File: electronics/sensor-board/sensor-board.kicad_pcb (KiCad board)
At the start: 2 copper layers, 270 x 30 mm, 0 parts

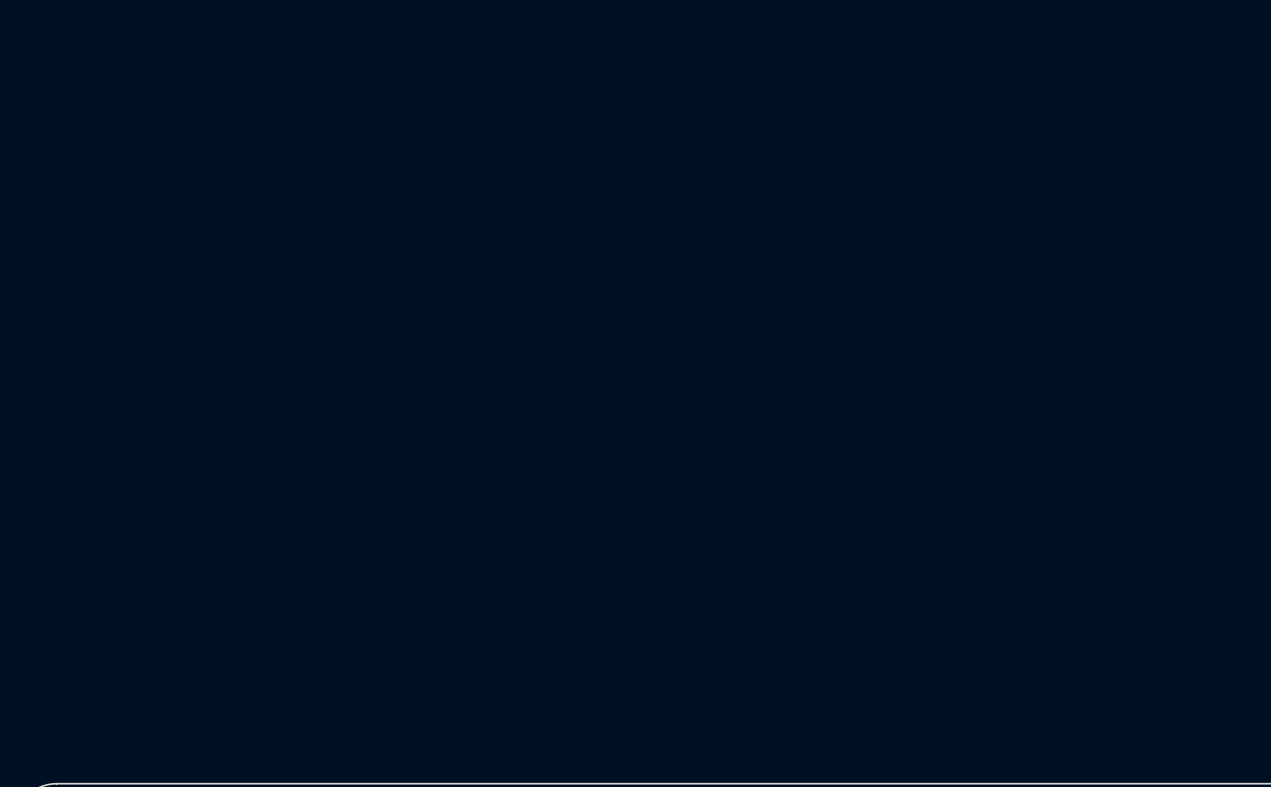
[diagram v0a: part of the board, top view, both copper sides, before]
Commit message: Minor tweaks, footprints added
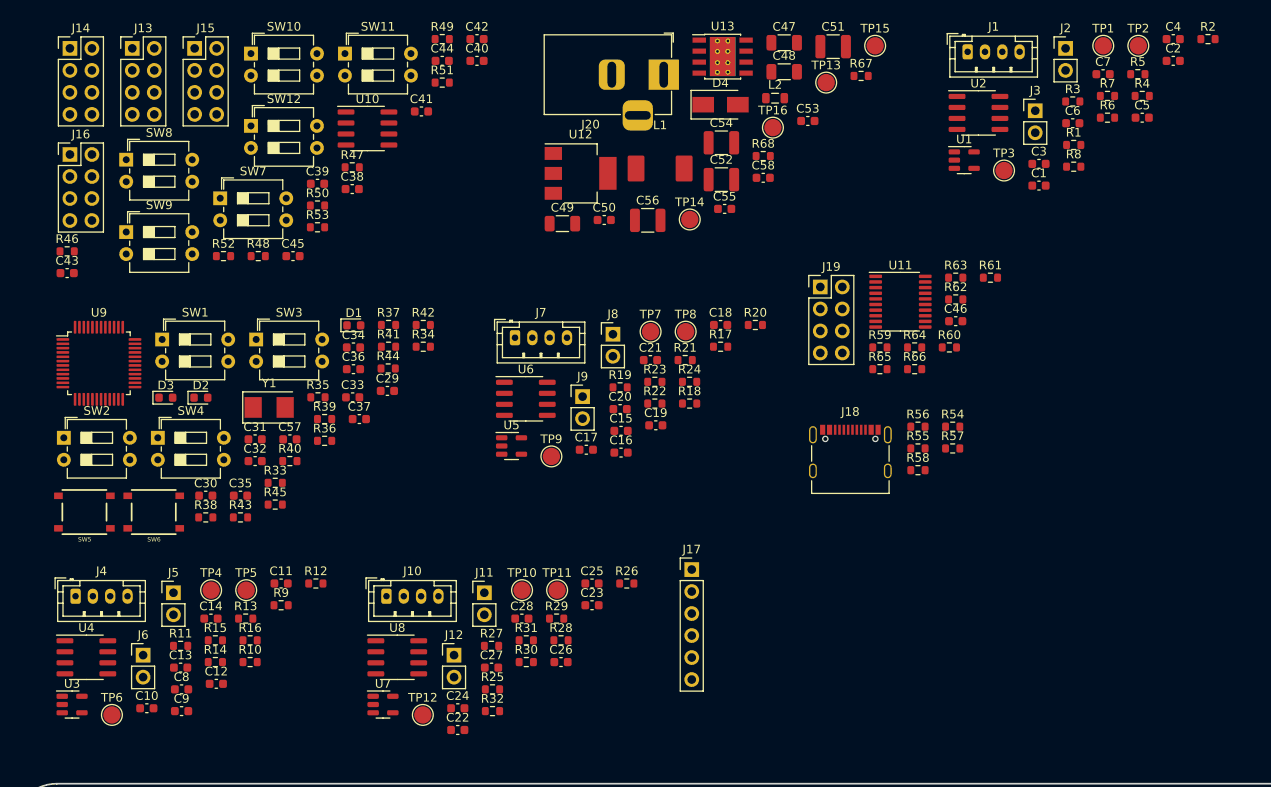
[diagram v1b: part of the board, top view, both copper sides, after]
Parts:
- added C1: 100n, Capacitor_SMD:C_0603_1608Metric, F.Cu at (196.0, 54.4)
- added C10: 4.7n, Capacitor_SMD:C_0603_1608Metric, F.Cu at (93.0, 114.7)
- added C11: 470n, Capacitor_SMD:C_0603_1608Metric, F.Cu at (108.5, 100.3)
- added C12: 4.7n, Capacitor_SMD:C_0603_1608Metric, F.Cu at (101.0, 111.9)
- added C13: 100n, Capacitor_SMD:C_0603_1608Metric, F.Cu at (96.9, 110.0)
- added C14: 10u, Capacitor_SMD:C_0603_1608Metric, F.Cu at (100.4, 104.3)
- added C15: 100n, Capacitor_SMD:C_0603_1608Metric, F.Cu at (147.7, 82.7)
- added C16: 100n, Capacitor_SMD:C_0603_1608Metric, F.Cu at (147.7, 85.2)
- added C17: 4.7n, Capacitor_SMD:C_0603_1608Metric, F.Cu at (143.7, 84.8)
- added C18: 470n, Capacitor_SMD:C_0603_1608Metric, F.Cu at (159.2, 70.5)
- added C19: 4.7n, Capacitor_SMD:C_0603_1608Metric, F.Cu at (151.7, 82.0)
- added C2: 100n, Capacitor_SMD:C_0603_1608Metric, F.Cu at (211.5, 40.0)
- added C20: 100n, Capacitor_SMD:C_0603_1608Metric, F.Cu at (147.6, 80.2)
- added C21: 10u, Capacitor_SMD:C_0603_1608Metric, F.Cu at (151.1, 74.5)
- added C22: 100n, Capacitor_SMD:C_0603_1608Metric, F.Cu at (128.9, 117.2)
- added C23: 100n, Capacitor_SMD:C_0603_1608Metric, F.Cu at (144.4, 102.8)
- added C24: 4.7n, Capacitor_SMD:C_0603_1608Metric, F.Cu at (128.9, 114.7)
- added C25: 470n, Capacitor_SMD:C_0603_1608Metric, F.Cu at (144.4, 100.3)
- added C26: 4.7n, Capacitor_SMD:C_0603_1608Metric, F.Cu at (140.8, 109.4)
- added C27: 100n, Capacitor_SMD:C_0603_1608Metric, F.Cu at (132.8, 110.0)
- added C28: 10u, Capacitor_SMD:C_0603_1608Metric, F.Cu at (136.3, 104.3)
- added C29: 22p, Capacitor_SMD:C_0603_1608Metric, F.Cu at (120.8, 78.1)
- added C3: 4.7n, Capacitor_SMD:C_0603_1608Metric, F.Cu at (196.0, 51.9)
- added C30: 22p, Capacitor_SMD:C_0603_1608Metric, F.Cu at (99.8, 90.2)
- added C31: 100n, Capacitor_SMD:C_0603_1608Metric, F.Cu at (105.5, 83.7)
- added C32: 100n, Capacitor_SMD:C_0603_1608Metric, F.Cu at (105.5, 86.2)
- added C33: 100n, Capacitor_SMD:C_0603_1608Metric, F.Cu at (116.7, 78.8)
- added C34: 470n, Capacitor_SMD:C_0603_1608Metric, F.Cu at (116.8, 73.0)
- added C35: 100n, Capacitor_SMD:C_0603_1608Metric, F.Cu at (103.8, 90.2)
- added C36: 100n, Capacitor_SMD:C_0603_1608Metric, F.Cu at (116.8, 75.5)
- added C37: 4.7u, Capacitor_SMD:C_0603_1608Metric, F.Cu at (117.5, 81.3)
- added C38: 100n, Capacitor_SMD:C_0603_1608Metric, F.Cu at (116.7, 54.8)
- added C39: 100n, Capacitor_SMD:C_0603_1608Metric, F.Cu at (112.7, 54.1)
- added C4: 470n, Capacitor_SMD:C_0603_1608Metric, F.Cu at (211.5, 37.5)
- added C40: 100p, Capacitor_SMD:C_0603_1608Metric, F.Cu at (131.1, 40.0)
- added C41: 4.7n, Capacitor_SMD:C_0603_1608Metric, F.Cu at (124.7, 45.8)
- added C42: 100p, Capacitor_SMD:C_0603_1608Metric, F.Cu at (131.1, 37.5)
- added C43: 100p, Capacitor_SMD:C_0603_1608Metric, F.Cu at (83.8, 64.5)
- added C44: 4.7n, Capacitor_SMD:C_0603_1608Metric, F.Cu at (127.1, 40.0)
- added C45: 100p, Capacitor_SMD:C_0603_1608Metric, F.Cu at (109.9, 62.5)
- added C46: 100n, Capacitor_SMD:C_0603_1608Metric, F.Cu at (186.4, 70.0)
- added C47: 10u, Capacitor_SMD:C_1206_3216Metric, F.Cu at (166.6, 37.9)
- added C48: 10u, Capacitor_SMD:C_1206_3216Metric, F.Cu at (166.6, 41.2)
- added C49: 22u, Capacitor_SMD:C_1206_3216Metric, F.Cu at (141.0, 58.8)
- added C5: 4.7n, Capacitor_SMD:C_0603_1608Metric, F.Cu at (207.9, 46.5)
- added C50: 100n, Capacitor_SMD:C_0603_1608Metric, F.Cu at (145.8, 58.3)
- added C51: 100u, Capacitor_SMD:C_1210_3225Metric, F.Cu at (172.2, 38.3)
- added C52: 100u, Capacitor_SMD:C_1210_3225Metric, F.Cu at (159.3, 53.7)
- added C53: 470n, Capacitor_SMD:C_0603_1608Metric, F.Cu at (169.3, 46.9)
- added C54: 100u, Capacitor_SMD:C_1210_3225Metric, F.Cu at (159.3, 49.4)
- added C55: 100n, Capacitor_SMD:C_0603_1608Metric, F.Cu at (159.7, 57.0)
- added C56: 100u, Capacitor_SMD:C_1210_3225Metric, F.Cu at (150.8, 58.4)
- added C57: 470n, Capacitor_SMD:C_0603_1608Metric, F.Cu at (109.5, 83.7)
- added C58: 470n, Capacitor_SMD:C_0603_1608Metric, F.Cu at (164.1, 53.5)
- added C6: 100n, Capacitor_SMD:C_0603_1608Metric, F.Cu at (199.9, 47.2)
- added C7: 10u, Capacitor_SMD:C_0603_1608Metric, F.Cu at (203.4, 41.5)
- added C8: 100n, Capacitor_SMD:C_0603_1608Metric, F.Cu at (97.0, 112.5)
- added C9: 100n, Capacitor_SMD:C_0603_1608Metric, F.Cu at (97.0, 115.0)
- added D1: Blue, LED_SMD:LED_0603_1608Metric, F.Cu at (116.9, 70.5)
- added D2: Green, LED_SMD:LED_0603_1608Metric, F.Cu at (99.2, 78.8)
- added D3: Yellow, LED_SMD:LED_0603_1608Metric, F.Cu at (95.2, 78.8)
- added D4: D_Schottky_Small, Diode_SMD:D_SMA, F.Cu at (159.2, 45.0)
- added J1: Load Cell Input, Connector_JST:JST_PH_B4B-PH-K_1x04_P2.00mm_Vertical, F.Cu at (187.7, 38.9)
- added J10: Load Cell Input, Connector_JST:JST_PH_B4B-PH-K_1x04_P2.00mm_Vertical, F.Cu at (120.6, 101.8)
- added J11: FSR Input, Connector_PinHeader_2.54mm:PinHeader_1x02_P2.54mm_Vertical, F.Cu at (131.9, 101.4)
- added J12: Digital Input, Connector_PinHeader_2.54mm:PinHeader_1x02_P2.54mm_Vertical, F.Cu at (128.4, 108.6)
- added J13: Conn_02x04_Counter_Clockwise, Connector_PinHeader_2.54mm:PinHeader_2x04_P2.54mm_Vertical, F.Cu at (91.3, 38.5)
- added J14: Conn_02x04_Counter_Clockwise, Connector_PinHeader_2.54mm:PinHeader_2x04_P2.54mm_Vertical, F.Cu at (84.1, 38.5)
- added J15: Conn_02x04_Counter_Clockwise, Connector_PinHeader_2.54mm:PinHeader_2x04_P2.54mm_Vertical, F.Cu at (98.5, 38.5)
- added J16: Conn_02x04_Counter_Clockwise, Connector_PinHeader_2.54mm:PinHeader_2x04_P2.54mm_Vertical, F.Cu at (84.1, 50.8)
- added J17: Conn_01x06_Male, Connector_PinHeader_2.54mm:PinHeader_1x06_P2.54mm_Vertical, F.Cu at (155.9, 98.7)
- added J18: USB_C_Receptacle_USB2.0, Connector_USB:USB_C_Receptacle_Palconn_UTC16-G, F.Cu at (174.2, 85.0)
- added J19: Conn_02x04_Counter_Clockwise, Connector_PinHeader_2.54mm:PinHeader_2x04_P2.54mm_Vertical, F.Cu at (170.7, 66.1)
- added J2: FSR Input, Connector_PinHeader_2.54mm:PinHeader_1x02_P2.54mm_Vertical, F.Cu at (199.0, 38.5)
- added J20: Barrel_Jack_MountingPin, Connector_BarrelJack:BarrelJack_Horizontal, F.Cu at (152.7, 41.6)
- added J3: Digital Input, Connector_PinHeader_2.54mm:PinHeader_1x02_P2.54mm_Vertical, F.Cu at (195.5, 45.7)
- added J4: Load Cell Input, Connector_JST:JST_PH_B4B-PH-K_1x04_P2.00mm_Vertical, F.Cu at (84.8, 101.8)
- added J5: FSR Input, Connector_PinHeader_2.54mm:PinHeader_1x02_P2.54mm_Vertical, F.Cu at (96.1, 101.4)
- added J6: Digital Input, Connector_PinHeader_2.54mm:PinHeader_1x02_P2.54mm_Vertical, F.Cu at (92.6, 108.6)
- added J7: Load Cell Input, Connector_JST:JST_PH_B4B-PH-K_1x04_P2.00mm_Vertical, F.Cu at (135.5, 71.9)
- added J8: FSR Input, Connector_PinHeader_2.54mm:PinHeader_1x02_P2.54mm_Vertical, F.Cu at (146.8, 71.5)
- added J9: Digital Input, Connector_PinHeader_2.54mm:PinHeader_1x02_P2.54mm_Vertical, F.Cu at (143.3, 78.7)
- added L1: 15u, sensor-board:SLO0630H150MTT, F.Cu at (152.2, 52.4)
- added L2: L_Ferrite_Small, Inductor_SMD:L_0805_2012Metric, F.Cu at (165.5, 44.3)
- added R1: 33k, Resistor_SMD:R_0603_1608Metric, F.Cu at (200.0, 49.7)
- added R10: 10k, Resistor_SMD:R_0603_1608Metric, F.Cu at (104.9, 109.4)
- added R11: 470R, Resistor_SMD:R_0603_1608Metric, F.Cu at (96.9, 107.5)
- added R12: 330R, Resistor_SMD:R_0603_1608Metric, F.Cu at (112.5, 100.3)
- added R13: 10k, Resistor_SMD:R_0603_1608Metric, F.Cu at (104.4, 104.3)
- added R14: 330R, Resistor_SMD:R_0603_1608Metric, F.Cu at (100.9, 109.4)
- added R15: 330R, Resistor_SMD:R_0603_1608Metric, F.Cu at (100.9, 106.8)
- added R16: 100R, Resistor_SMD:R_0603_1608Metric, F.Cu at (104.9, 106.8)
- added R17: 33k, Resistor_SMD:R_0603_1608Metric, F.Cu at (159.2, 73.0)
- added R18: 10k, Resistor_SMD:R_0603_1608Metric, F.Cu at (155.6, 79.5)
- added R19: 470R, Resistor_SMD:R_0603_1608Metric, F.Cu at (147.6, 77.7)
- added R2: 10k, Resistor_SMD:R_0603_1608Metric, F.Cu at (215.5, 37.5)
- added R20: 330R, Resistor_SMD:R_0603_1608Metric, F.Cu at (163.2, 70.5)
- added R21: 10k, Resistor_SMD:R_0603_1608Metric, F.Cu at (155.1, 74.5)
- added R22: 330R, Resistor_SMD:R_0603_1608Metric, F.Cu at (151.6, 79.5)
- added R23: 330R, Resistor_SMD:R_0603_1608Metric, F.Cu at (151.6, 77.0)
- added R24: 100R, Resistor_SMD:R_0603_1608Metric, F.Cu at (155.6, 77.0)
- added R25: 33k, Resistor_SMD:R_0603_1608Metric, F.Cu at (132.9, 112.5)
- added R26: 10k, Resistor_SMD:R_0603_1608Metric, F.Cu at (148.4, 100.3)
- added R27: 470R, Resistor_SMD:R_0603_1608Metric, F.Cu at (132.8, 107.5)
- added R28: 330R, Resistor_SMD:R_0603_1608Metric, F.Cu at (140.8, 106.8)
- added R29: 10k, Resistor_SMD:R_0603_1608Metric, F.Cu at (140.3, 104.3)
- added R3: 470R, Resistor_SMD:R_0603_1608Metric, F.Cu at (199.9, 44.6)
- added R30: 330R, Resistor_SMD:R_0603_1608Metric, F.Cu at (136.8, 109.4)
- added R31: 330R, Resistor_SMD:R_0603_1608Metric, F.Cu at (136.8, 106.8)
- added R32: 100R, Resistor_SMD:R_0603_1608Metric, F.Cu at (132.9, 115.0)
- added R33: 10k, Resistor_SMD:R_0603_1608Metric, F.Cu at (107.8, 88.7)
- added R34: 10k, Resistor_SMD:R_0603_1608Metric, F.Cu at (124.9, 73.0)
- added R35: 10k, Resistor_SMD:R_0603_1608Metric, F.Cu at (112.7, 78.8)
- added R36: 10k, Resistor_SMD:R_0603_1608Metric, F.Cu at (113.5, 83.8)
- added R37: 10k, Resistor_SMD:R_0603_1608Metric, F.Cu at (120.9, 70.5)
- added R38: 10k, Resistor_SMD:R_0603_1608Metric, F.Cu at (99.8, 92.7)
- added R39: 10k, Resistor_SMD:R_0603_1608Metric, F.Cu at (113.5, 81.3)
- added R4: 330R, Resistor_SMD:R_0603_1608Metric, F.Cu at (207.9, 44.0)
- added R40: 10k, Resistor_SMD:R_0603_1608Metric, F.Cu at (109.5, 86.2)
- added R41: 10k, Resistor_SMD:R_0603_1608Metric, F.Cu at (120.9, 73.0)
- added R42: 47R, Resistor_SMD:R_0603_1608Metric, F.Cu at (124.9, 70.5)
- added R43: 56R, Resistor_SMD:R_0603_1608Metric, F.Cu at (103.8, 92.7)
- added R44: 120R, Resistor_SMD:R_0603_1608Metric, F.Cu at (120.8, 75.5)
- added R45: 220R, Resistor_SMD:R_0603_1608Metric, F.Cu at (107.8, 91.2)
- added R46: 27R, Resistor_SMD:R_0603_1608Metric, F.Cu at (83.8, 62.0)
- added R47: 27R, Resistor_SMD:R_0603_1608Metric, F.Cu at (116.7, 52.2)
- added R48: 33R, Resistor_SMD:R_0603_1608Metric, F.Cu at (105.8, 62.5)
- added R49: 33R, Resistor_SMD:R_0603_1608Metric, F.Cu at (127.1, 37.5)
- added R5: 10k, Resistor_SMD:R_0603_1608Metric, F.Cu at (207.4, 41.5)
- added R50: 27R, Resistor_SMD:R_0603_1608Metric, F.Cu at (112.7, 56.7)
- added R51: 27R, Resistor_SMD:R_0603_1608Metric, F.Cu at (127.1, 42.5)
- added R52: 33R, Resistor_SMD:R_0603_1608Metric, F.Cu at (101.8, 62.5)
- added R53: 33R, Resistor_SMD:R_0603_1608Metric, F.Cu at (112.7, 59.2)
- added R54: 5.1k, Resistor_SMD:R_0603_1608Metric, F.Cu at (186.0, 82.2)
- added R55: 5.1k, Resistor_SMD:R_0603_1608Metric, F.Cu at (182.0, 84.7)
- added R56: 1.5k, Resistor_SMD:R_0603_1608Metric, F.Cu at (182.0, 82.2)
- added R57: 22R, Resistor_SMD:R_0603_1608Metric, F.Cu at (186.0, 84.7)
- added R58: 22R, Resistor_SMD:R_0603_1608Metric, F.Cu at (182.0, 87.2)
- added R59: 10k, Resistor_SMD:R_0603_1608Metric, F.Cu at (177.6, 73.0)
- added R6: 330R, Resistor_SMD:R_0603_1608Metric, F.Cu at (203.9, 46.5)
- added R60: 10k, Resistor_SMD:R_0603_1608Metric, F.Cu at (185.6, 73.0)
- added R61: 10k, Resistor_SMD:R_0603_1608Metric, F.Cu at (190.4, 65.0)
- added R62: 10k, Resistor_SMD:R_0603_1608Metric, F.Cu at (186.4, 67.5)
- added R63: 10k, Resistor_SMD:R_0603_1608Metric, F.Cu at (186.4, 65.0)
- added R64: 10k, Resistor_SMD:R_0603_1608Metric, F.Cu at (181.6, 73.0)
- added R65: 10k, Resistor_SMD:R_0603_1608Metric, F.Cu at (177.6, 75.5)
- added R66: 10k, Resistor_SMD:R_0603_1608Metric, F.Cu at (181.6, 75.5)
- added R67: 10k, Resistor_SMD:R_0603_1608Metric, F.Cu at (175.4, 41.7)
- added R68: 3.3k, Resistor_SMD:R_0603_1608Metric, F.Cu at (164.1, 51.0)
- added R7: 330R, Resistor_SMD:R_0603_1608Metric, F.Cu at (203.9, 44.0)
- added R8: 100R, Resistor_SMD:R_0603_1608Metric, F.Cu at (200.0, 52.2)
- added R9: 33k, Resistor_SMD:R_0603_1608Metric, F.Cu at (108.5, 102.8)
- added SW1: SW_DIP_x02, Button_Switch_THT:SW_DIP_SPSTx02_Slide_6.7x6.64mm_W7.62mm_P2.54mm_LowProfile, F.Cu at (94.8, 72.1)
- added SW10: SW_DIP_x02, Button_Switch_THT:SW_DIP_SPSTx02_Slide_6.7x6.64mm_W7.62mm_P2.54mm_LowProfile, F.Cu at (105.0, 39.1)
- added SW11: SW_DIP_x02, Button_Switch_THT:SW_DIP_SPSTx02_Slide_6.7x6.64mm_W7.62mm_P2.54mm_LowProfile, F.Cu at (115.9, 39.1)
- added SW12: SW_DIP_x02, Button_Switch_THT:SW_DIP_SPSTx02_Slide_6.7x6.64mm_W7.62mm_P2.54mm_LowProfile, F.Cu at (105.0, 47.5)
- added SW2: SW_DIP_x02, Button_Switch_THT:SW_DIP_SPSTx02_Slide_6.7x6.64mm_W7.62mm_P2.54mm_LowProfile, F.Cu at (83.4, 83.5)
- added SW3: SW_DIP_x02, Button_Switch_THT:SW_DIP_SPSTx02_Slide_6.7x6.64mm_W7.62mm_P2.54mm_LowProfile, F.Cu at (105.6, 72.1)
- added SW4: SW_DIP_x02, Button_Switch_THT:SW_DIP_SPSTx02_Slide_6.7x6.64mm_W7.62mm_P2.54mm_LowProfile, F.Cu at (94.3, 83.5)
- added SW5: SW_Push, sensor-board:TS-1187A-B-A-B, F.Cu at (85.8, 92.0)
- added SW6: SW_Push, sensor-board:TS-1187A-B-A-B, F.Cu at (93.8, 92.0)
- added SW7: SW_DIP_x02, Button_Switch_THT:SW_DIP_SPSTx02_Slide_6.7x6.64mm_W7.62mm_P2.54mm_LowProfile, F.Cu at (101.5, 55.8)
- added SW8: SW_DIP_x02, Button_Switch_THT:SW_DIP_SPSTx02_Slide_6.7x6.64mm_W7.62mm_P2.54mm_LowProfile, F.Cu at (90.6, 51.4)
- added SW9: SW_DIP_x02, Button_Switch_THT:SW_DIP_SPSTx02_Slide_6.7x6.64mm_W7.62mm_P2.54mm_LowProfile, F.Cu at (90.6, 59.7)
- added TP1: TestPoint, TestPoint:TestPoint_Pad_D2.0mm, F.Cu at (203.4, 38.2)
- added TP10: TestPoint, TestPoint:TestPoint_Pad_D2.0mm, F.Cu at (136.3, 101.1)
- added TP11: TestPoint, TestPoint:TestPoint_Pad_D2.0mm, F.Cu at (140.3, 101.1)
- added TP12: TestPoint, TestPoint:TestPoint_Pad_D2.0mm, F.Cu at (124.8, 115.5)
- added TP13: TestPoint, TestPoint:TestPoint_Pad_D2.0mm, F.Cu at (171.4, 42.5)
- added TP14: TestPoint, TestPoint:TestPoint_Pad_D2.0mm, F.Cu at (155.7, 58.3)
- added TP15: TestPoint, TestPoint:TestPoint_Pad_D2.0mm, F.Cu at (177.1, 38.2)
- added TP16: TestPoint, TestPoint:TestPoint_Pad_D2.0mm, F.Cu at (165.3, 47.7)
- added TP2: TestPoint, TestPoint:TestPoint_Pad_D2.0mm, F.Cu at (207.4, 38.2)
- added TP3: TestPoint, TestPoint:TestPoint_Pad_D2.0mm, F.Cu at (191.9, 52.6)
- added TP4: TestPoint, TestPoint:TestPoint_Pad_D2.0mm, F.Cu at (100.4, 101.1)
- added TP5: TestPoint, TestPoint:TestPoint_Pad_D2.0mm, F.Cu at (104.5, 101.1)
- added TP6: TestPoint, TestPoint:TestPoint_Pad_D2.0mm, F.Cu at (89.0, 115.5)
- added TP7: TestPoint, TestPoint:TestPoint_Pad_D2.0mm, F.Cu at (151.1, 71.2)
- added TP8: TestPoint, TestPoint:TestPoint_Pad_D2.0mm, F.Cu at (155.2, 71.2)
- added TP9: TestPoint, TestPoint:TestPoint_Pad_D2.0mm, F.Cu at (139.7, 85.6)
- added U1: LMV321, Package_TO_SOT_SMD:SOT-23-5, F.Cu at (187.3, 51.4)
- added U10: TJA1042T-3, Package_SO:SOIC-8_3.9x4.9mm_P1.27mm, F.Cu at (118.5, 47.8)
- added U11: 74HCT245, Package_SO:TSSOP-20_4.4x6.5mm_P0.65mm, F.Cu at (180.0, 67.8)
- added U12: AMS1117-3.3, Package_TO_SOT_SMD:SOT-223-3_TabPin2, F.Cu at (143.1, 53.0)
- added U13: TPS5430DDA, Package_SO:TI_SO-PowerPAD-8_ThermalVias, F.Cu at (159.5, 39.5)
- added U2: INA826, Package_SO:SOIC-8_3.9x4.9mm_P1.27mm, F.Cu at (189.0, 46.0)
- added U3: LMV321, Package_TO_SOT_SMD:SOT-23-5, F.Cu at (84.4, 114.3)
- added U4: INA826, Package_SO:SOIC-8_3.9x4.9mm_P1.27mm, F.Cu at (86.0, 108.8)
- added U5: LMV321, Package_TO_SOT_SMD:SOT-23-5, F.Cu at (135.1, 84.4)
- added U6: INA826, Package_SO:SOIC-8_3.9x4.9mm_P1.27mm, F.Cu at (136.7, 79.0)
- added U7: LMV321, Package_TO_SOT_SMD:SOT-23-5, F.Cu at (120.2, 114.3)
- added U8: INA826, Package_SO:SOIC-8_3.9x4.9mm_P1.27mm, F.Cu at (121.9, 108.8)
- added U9: STM32F302C8Tx, Package_QFP:LQFP-48_7x7mm_P0.5mm, F.Cu at (87.5, 74.9)
- added Y1: 8MHz, Crystal:Crystal_SMD_5032-2Pin_5.0x3.2mm, F.Cu at (107.1, 80.0)

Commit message: Final tweaks and schematic review complete
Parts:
- removed C57, C58: 470n, Capacitor_SMD:C_0603_1608Metric
- added H1: MountingHole_Pad, MountingHole:MountingHole_3.2mm_M3_Pad, F.Cu at (111.4, 56.3)
- added H2: MountingHole_Pad, MountingHole:MountingHole_3.2mm_M3_Pad, F.Cu at (119.1, 48.4)
- added H3: MountingHole_Pad, MountingHole:MountingHole_3.2mm_M3_Pad, F.Cu at (103.4, 60.6)
- added H4: MountingHole_Pad, MountingHole:MountingHole_3.2mm_M3_Pad, F.Cu at (125.0, 40.0)
- C34, C53: value 470n -> 1u
- J13, J14, J15, J16, J19: value Conn_02x04_Counter_Clockwise -> Conn_02x04_Odd_Even
- J20: footprint Connector_BarrelJack:BarrelJack_Horizontal -> sensor-board:BarrelJack_MP
- moved J17 54.1 mm to (194.7, 61.0)
- moved R49 43.4 mm to (94.6, 66.2)
- moved C42 37.5 mm to (106.7, 65.8)
- moved SW10 35.3 mm to (79.4, 63.5)
- moved R34 28.3 mm to (103.8, 91.8)
- moved D1 28.1 mm to (91.2, 81.9)
- moved C45 25.8 mm to (129.1, 45.2)
- moved R43 25.6 mm to (120.9, 73.5)
- moved C39 24.9 mm to (131.0, 37.3)
- moved R46 24.0 mm to (101.4, 45.6)
- moved J15 22.0 mm to (80.1, 50.6)
- moved C41 21.9 mm to (109.4, 61.5)
- moved SW1 21.1 mm to (79.4, 86.5)
- moved R44 20.6 mm to (105.5, 89.2)
- moved SW12 18.8 mm to (86.6, 51.2)
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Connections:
- J13 pad 2: +24V -> Net-(J13-Pad2)
- J13 pad 3: GND -> +24V
- J13 pad 4: GND -> Net-(J13-Pad4)
- J13 pad 5: /pad_bus/CANL -> GND
- J13 pad 7: Net-(J13-Pad7) -> GND
- J13 pad 8: Net-(J13-Pad8) -> /pad_bus/CANL
- J14 pad 2: +24V -> /pad_bus/CANH
- J14 pad 3: GND -> +24V
- J14 pad 4: GND -> /pad_bus/CANL
- J14 pad 5: Net-(J14-Pad5) -> GND
- J14 pad 7: /pad_bus/CANL -> GND
- J14 pad 8: /pad_bus/CANH -> Net-(J14-Pad8)
- J15 pad 2: +24V -> Net-(J14-Pad6)
- J15 pad 3: GND -> +24V
- J15 pad 4: GND -> Net-(J14-Pad8)
- J15 pad 5: Net-(J15-Pad5) -> GND
- J15 pad 7: Net-(J14-Pad5) -> GND
- J15 pad 8: Net-(J14-Pad6) -> Net-(J15-Pad8)
- J16 pad 2: +24V -> Net-(J15-Pad6)
- J16 pad 3: GND -> +24V
- J16 pad 4: GND -> Net-(J15-Pad8)
- J16 pad 5: Net-(J13-Pad7) -> GND
- J16 pad 6: Net-(J13-Pad8) -> Net-(J13-Pad2)
- J16 pad 7: Net-(J15-Pad5) -> GND
- J16 pad 8: Net-(J15-Pad6) -> Net-(J13-Pad4)
- J19 pad 2: Net-(J19-Pad2) -> +5V
- J19 pad 4: Net-(J19-Pad4) -> +5V
- J19 pad 5: GND -> Net-(J19-Pad5)
- J19 pad 7: +5V -> Net-(J19-Pad7)
- J19 pad 8: +5V -> GND
- R13 pad 1: +3.3V -> +3.3VA
- R21 pad 1: +3.3V -> +3.3VA
- R29 pad 1: +3.3V -> +3.3VA
- R5 pad 1: +3.3V -> +3.3VA
- SW10 pad 2: Net-(J15-Pad5) -> Net-(J15-Pad8)
- SW10 pad 3: Net-(J13-Pad7) -> Net-(J13-Pad4)
- SW10 pad 4: Net-(J13-Pad8) -> Net-(J13-Pad2)
- SW11 pad 1: Net-(J13-Pad8) -> Net-(J13-Pad2)
- SW11 pad 2: Net-(J13-Pad7) -> Net-(J13-Pad4)
- SW7 pad 1: Net-(J13-Pad8) -> Net-(J13-Pad2)
- SW7 pad 2: Net-(J13-Pad7) -> Net-(J13-Pad4)
- SW8 pad 3: Net-(J14-Pad5) -> Net-(J14-Pad8)
- SW9 pad 2: Net-(J14-Pad5) -> Net-(J14-Pad8)
- SW9 pad 3: Net-(J15-Pad5) -> Net-(J15-Pad8)
- U11 pad 15: Net-(J19-Pad4) -> Net-(J19-Pad7)
- U11 pad 16: Net-(J19-Pad3) -> Net-(J19-Pad5)
- U11 pad 17: Net-(J19-Pad2) -> Net-(J19-Pad3)

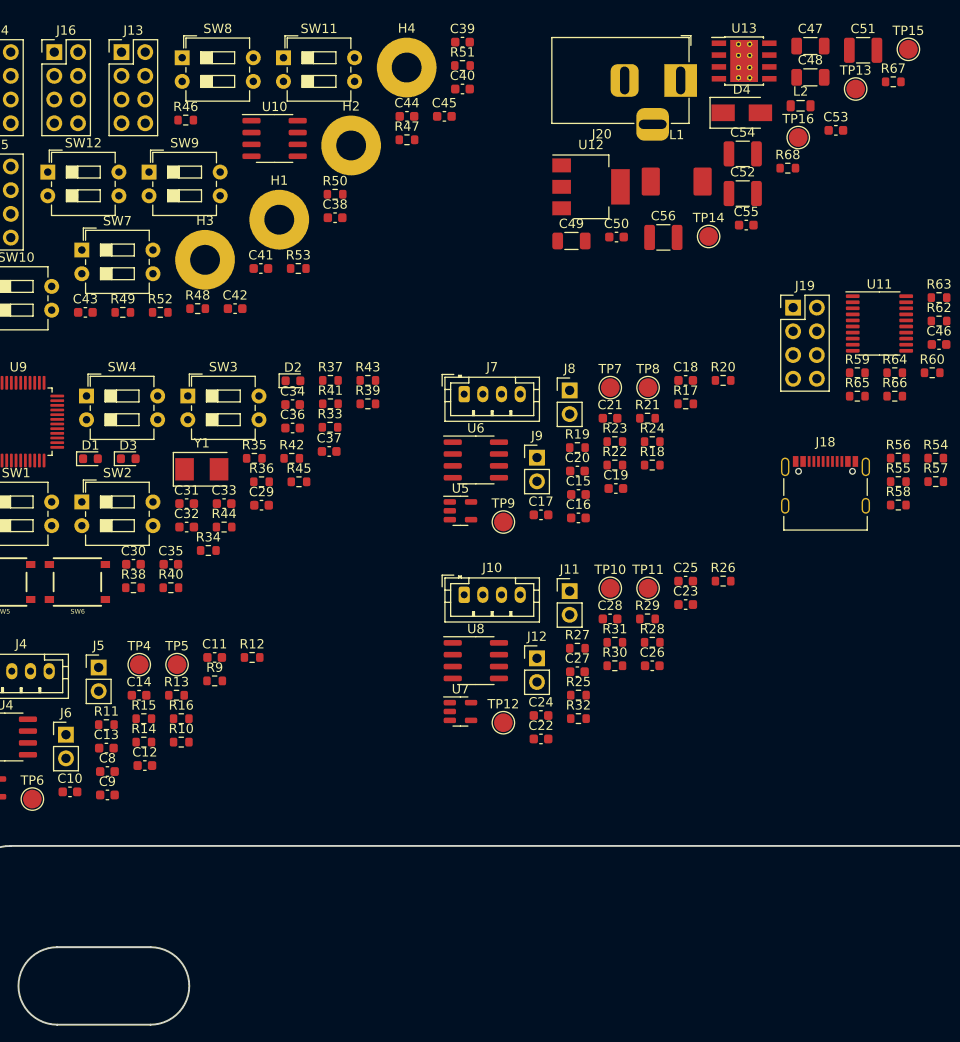
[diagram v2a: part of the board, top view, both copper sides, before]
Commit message: Set up board rules w/ controlled impedance
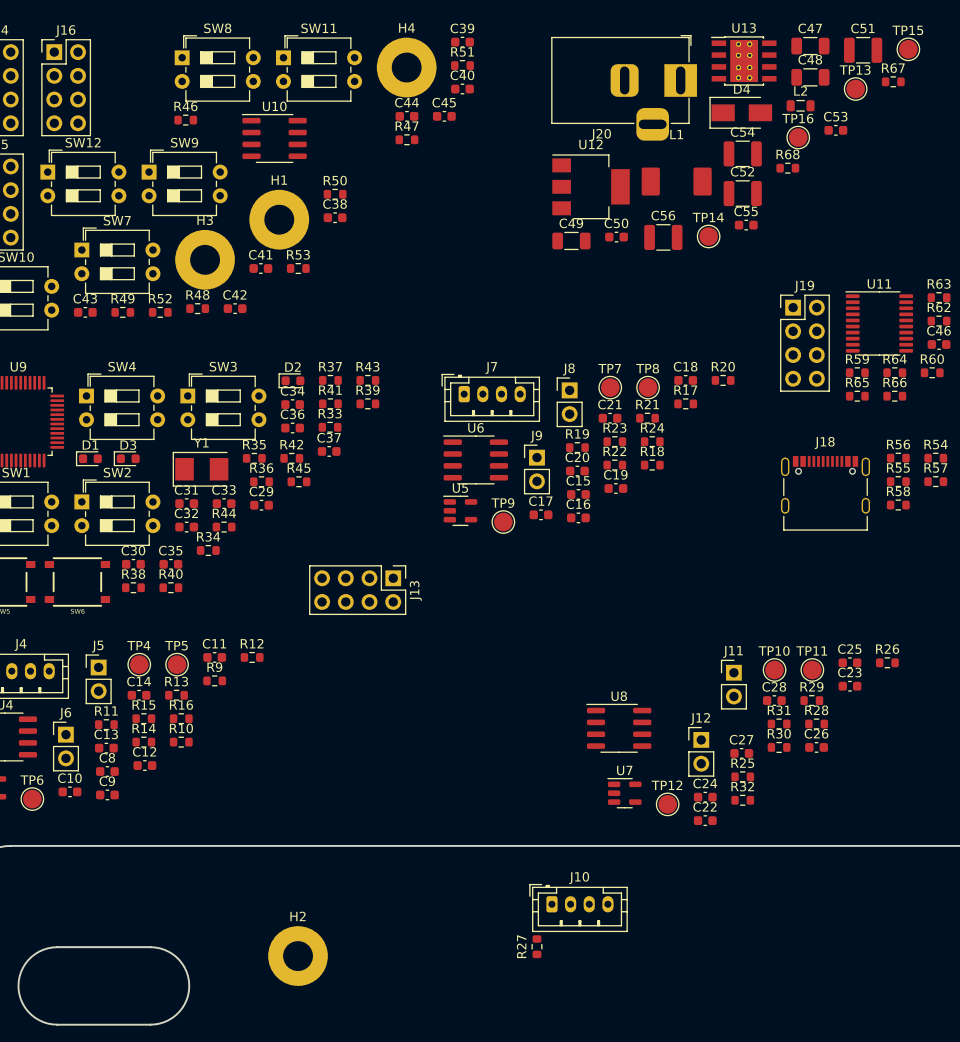
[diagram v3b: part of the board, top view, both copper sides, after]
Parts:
- moved H2 87.0 mm to (113.4, 135.2)
- moved J13 63.4 mm to (123.6, 94.7), turned to -90 degrees
- moved J10 34.5 mm to (140.6, 129.7)
- moved R27 32.3 mm to (139.0, 134.2), turned to 90 degrees
- moved C22 19.7 mm to (157.0, 120.7)
- moved C23 19.7 mm to (172.5, 106.3)
- moved C24 19.7 mm to (157.0, 118.2)
- moved C25 19.7 mm to (172.5, 103.8)
- moved C26 19.7 mm to (168.9, 112.8)
- moved C27 19.7 mm to (160.9, 113.5)
- moved C28 19.7 mm to (164.4, 107.8)
- moved J11 19.7 mm to (160.1, 104.8)
- moved J12 19.7 mm to (156.6, 112.0)
- moved R25 19.7 mm to (161.0, 116.0)
- moved R26 19.7 mm to (176.5, 103.8)
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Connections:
- net /controller/USB_DM renamed /controller/USBD_N
- net /controller/USB_DP renamed /controller/USBD_P
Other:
- copper layers 2 -> 4

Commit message: Preliminary sensor layout
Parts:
- moved J16 245.8 mm to (310.1, 142.2), turned to 180 degrees
- moved SW10 233.8 mm to (299.6, 142.2), turned to 90 degrees
- moved H4 214.5 mm to (315.6, 138.4)
- moved J5 199.8 mm to (290.2, 129.9)
- moved TP4 198.7 mm to (293.6, 128.5)
- moved J4 198.5 mm to (277.2, 132.9), turned to 180 degrees
- moved J6 195.6 mm to (283.0, 132.5), turned to 180 degrees
- moved R13 187.7 mm to (286.4, 132.6), turned to 180 degrees
- moved TP5 187.6 mm to (286.4, 128.5)
- moved R12 187.4 mm to (293.6, 132.6)
- moved R11 187.0 mm to (279.0, 128.0), turned to -90 degrees
- moved C8 184.8 mm to (277.4, 128.0), turned to -90 degrees
- moved U3 184.1 mm to (263.8, 132.4), turned to -90 degrees
- moved C10 183.2 mm to (271.8, 128.8), turned to 180 degrees
- moved U4 181.9 mm to (263.2, 127.4), turned to 180 degrees
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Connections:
- C3 pad 2: Net-(C3-Pad2) -> Net-(C10-Pad2)
- C4 pad 1: Net-(C3-Pad2) -> Net-(C10-Pad2)
- C4 pad 2: Net-(C4-Pad2) -> Net-(C11-Pad2)
- C5 pad 1: Net-(C4-Pad2) -> Net-(C11-Pad2)
- J1 pad 1: Net-(J1-Pad1) -> Net-(J4-Pad1)
- J1 pad 3: /sensor_handler1/SENSE+ -> /sensor_handler2/SENSE+
- J1 pad 4: /sensor_handler1/SENSE- -> /sensor_handler2/SENSE-
- J2 pad 2: /controller/FSR_UL -> /controller/FSR_UR
- J3 pad 1: /controller/DIGITALSENSOR_UL -> /controller/DIGITALSENSOR_UR
- R1 pad 2: Net-(R1-Pad2) -> Net-(R10-Pad1)
- R2 pad 1: Net-(R1-Pad2) -> Net-(R10-Pad1)
- R3 pad 2: Net-(J1-Pad1) -> Net-(J4-Pad1)
- R4 pad 1: /controller/FSR_UL -> /controller/FSR_UR
- R5 pad 2: /controller/DIGITALSENSOR_UL -> /controller/DIGITALSENSOR_UR
- R6 pad 1: /sensor_handler1/SENSE- -> /sensor_handler2/SENSE-
- R6 pad 2: Net-(C3-Pad2) -> Net-(C10-Pad2)
- R7 pad 1: /sensor_handler1/SENSE+ -> /sensor_handler2/SENSE+
- R7 pad 2: Net-(C4-Pad2) -> Net-(C11-Pad2)
- R8 pad 1: Net-(R8-Pad1) -> Net-(R16-Pad1)
- R8 pad 2: Net-(R8-Pad2) -> Net-(R16-Pad2)
- TP1 pad 1: /controller/FSR_UL -> /controller/FSR_UR
- TP2 pad 1: /controller/DIGITALSENSOR_UL -> /controller/DIGITALSENSOR_UR
- TP3 pad 1: /controller/LOADCELL_UL -> /controller/LOADCELL_UR
- TP7 pad 1: /controller/FSR_DL -> /controller/DIGITALSENSOR_DL
- U1 pad 1: Net-(R1-Pad2) -> Net-(R10-Pad1)
- U1 pad 3: /sensor_handler1/VREF -> /sensor_handler2/VREF
- U1 pad 4: /sensor_handler1/VREF -> /sensor_handler2/VREF
- U2 pad 1: Net-(C3-Pad2) -> Net-(C10-Pad2)
- U2 pad 2: Net-(R8-Pad1) -> Net-(R16-Pad1)
- U2 pad 3: Net-(R8-Pad2) -> Net-(R16-Pad2)
- U2 pad 4: Net-(C4-Pad2) -> Net-(C11-Pad2)
- U2 pad 6: /sensor_handler1/VREF -> /sensor_handler2/VREF
- U2 pad 7: /controller/LOADCELL_UL -> /controller/LOADCELL_UR
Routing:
- net /controller/FSR_UR: track 0.00 -> 59.0 mm
- net /controller/DIGITALSENSOR_UR: track 0.00 -> 59.0 mm
- net +3.3VA: track 0.00 -> 54.2 mm, vias 0 -> 28
- net GND: track 0.00 -> 53.2 mm, vias 0 -> 36
- net /controller/LOADCELL_UR: track 0.00 -> 51.5 mm
- net /controller/FSR_DR: track 0.00 -> 46.6 mm
- net /controller/LOADCELL_DL: track 0.00 -> 44.7 mm
- net /controller/DIGITALSENSOR_DR: track 0.00 -> 39.3 mm
- net Net-(C11-Pad2): track 0.00 -> 26.0 mm
- net Net-(C10-Pad2): track 0.00 -> 22.0 mm
- net /controller/DIGITALSENSOR_DL: track 0.00 -> 19.9 mm
- net /sensor_handler2/VREF: track 0.00 -> 17.2 mm
- net Net-(C18-Pad2): track 0.00 -> 13.0 mm
- net Net-(C25-Pad2): track 0.00 -> 13.0 mm
- net /controller/FSR_DL: track 0.00 -> 12.5 mm
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- added copper zone on In1.Cu, net +3.3VA
- added copper zone on In2.Cu, net GND
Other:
- board text added: "DIG- DIG+"
- board text added: "Digital"
- board text added: "Down-Left / Left Sensor"
- board text added: "Down-Right / Down Sensor"
- board text added: "FSR"
- board text added: "FSR+ FSR-"
- board text added: "Load Cell"
- board text added: "OFF"
- board text added: "ON"
- board text added: "Up-Left / Up Sensor"
- board text added: "Up-Right / Right Sensor"
